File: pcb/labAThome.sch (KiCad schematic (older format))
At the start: 107 parts, among them J1 I2C, J11 24.5.GND.3, J12 NEOPIXEL, J13 Power Input 1, J14 Conn_Coaxial, J15 WS2812_OUT, J2 SRVx, J3 5V, J4 EXT, J5 VPS, J6 FAN2, J7 1wire, J8 1wire, J9 FAN1, K1 G5V-2, K2 G5V-2, K3 G5V-2, M3 SN65HVD230_MODULE, Q1 BC847, Q2 IRLZ44N, Q3 IRLML6344, Q4 BC847, Q5 IRF530, Q6 IRLML5203, SW1 RED, SW2 GREEN, SW4 BLUE, SW5 WHITE, SW7 ROTENC, U1 SR602, U10 MAX3485_MODULE, U11 AM312, U12 24V->4V, U13 LM358, U14 MS4525DO, U15 CCS811_MODULE, U16 24V->5V, U17 DS18B20, U2 TPS5430DDA, U3 Power Input 2, U4 ESP32_DEVKITC_COMPATIBLE, U6 GY-302, U7 Display, U8 MIC, U9 RFM95W-868S2, X1 FAN_6024, m1 Attribution

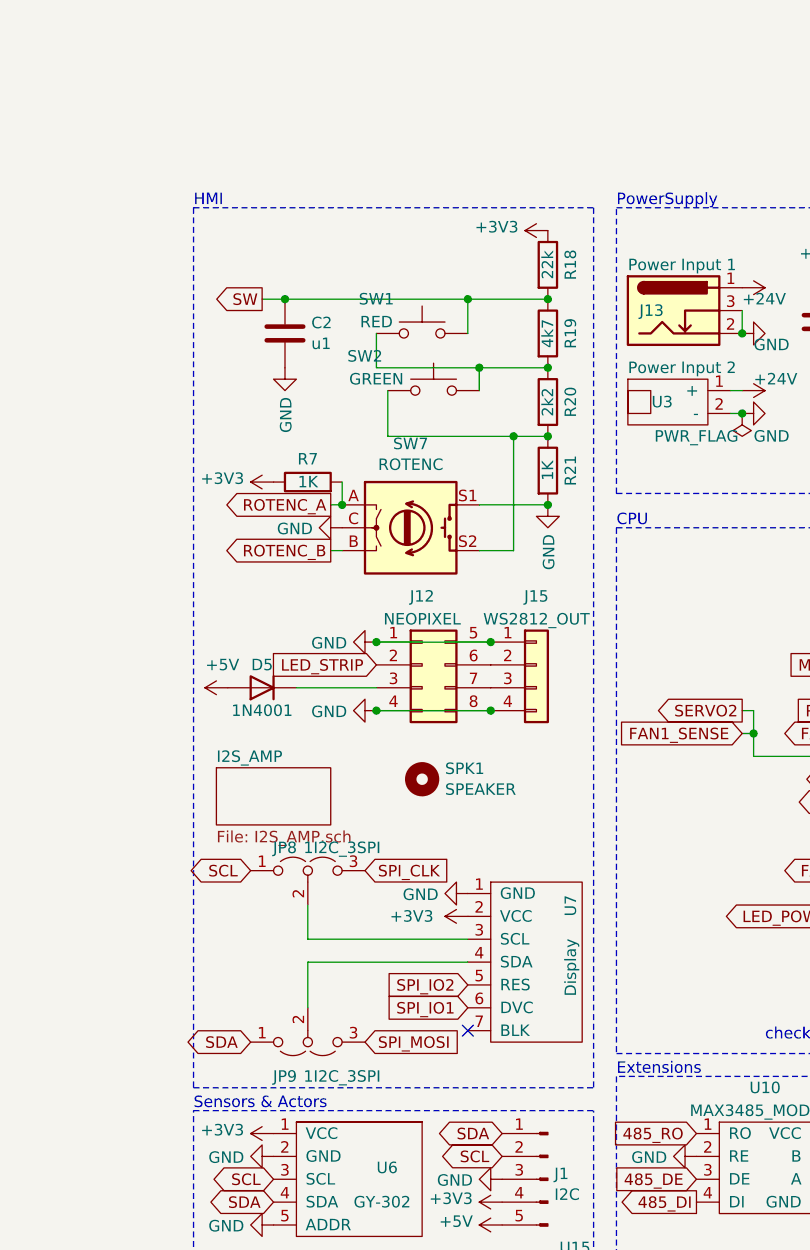
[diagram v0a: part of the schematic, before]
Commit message: I2S-Amp --> Analog (damn cheap) Amp
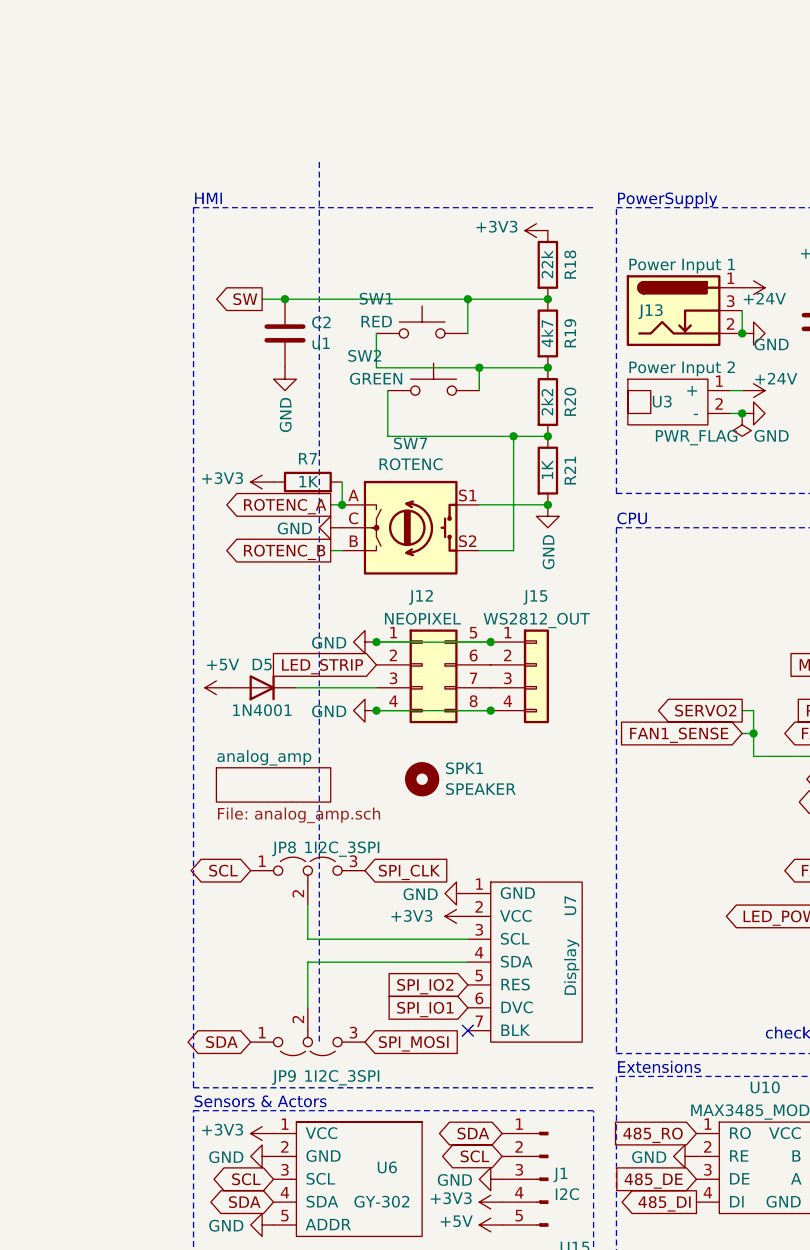
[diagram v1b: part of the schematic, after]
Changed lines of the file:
@@
 $EndComp
 Wire Notes Line
-	2300 600  2300 4450
+	1100 400  1100 4250
 Wire Notes Line
 	550  600  550  4450
@@
 1wire
 $Sheet
-S 650  3050 500  250
-U 60B80D3E
-F0 "I2S_AMP" 50
-F1 "I2S_AMP.sch" 50
+S 650  3050 500  150
+U 60B762EC
+F0 "analog_amp" 50
+F1 "analog_amp.sch" 50
 $EndSheet
 $EndSCHEMATC

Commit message: Minor PCB update
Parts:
- added C15: 100u, liebler_PASSIVES:CP_Elec_6.3x7.7_handsolder, symbol Device:CP
- J12: footprint smopla:NEOPIXEL_STICK_alternativ -> liebler_MODULES:NEOPIXEL_STICK
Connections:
- net GND: now also C15.2
- net at J12.7 (Pin_7), J15.3 (Pin_3): now also C15.1
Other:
- moved on the sheet: D5
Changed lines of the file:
@@
 	1    0    0    -1
 $EndComp
-Wire Notes Line
-	-2800 1850 -2800 5550
 $Comp
 L power:GND #PWR0109
@@
 L power:+5V #PWR051
 U 1 1 5EFC1FD4
-P 700 2700
-F 0 "#PWR051" H 700 2550 50  0001 C CNN
-F 1 "+5V" V 800 2650 50  0000 L CNN
-F 2 "" H 700 2700 50  0001 C CNN
-F 3 "" H 700 2700 50  0001 C CNN
-	1    700  2700
-	0    -1   -1   0
+P 700 2400
+F 0 "#PWR051" H 700 2250 50  0001 C CNN
+F 1 "+5V" V 800 2350 50  0000 L CNN
+F 2 "" H 700 2400 50  0001 C CNN
+F 3 "" H 700 2400 50  0001 C CNN
+	1    700  2400
+	1    0    0    -1
 $EndComp
 $Comp
@@
 P 1350 2800
 F 0 "#PWR052" H 1350 2550 50  0001 C CNN
-F 1 "GND" V 1355 2672 50  0000 R CNN
+F 1 "GND" H 1300 2750 50  0000 R CNN
 F 2 "" H 1350 2800 50  0001 C CNN
 F 3 "" H 1350 2800 50  0001 C CNN
 	1    1350 2800
-	0    1    1    0
+	1    0    0    -1
 $EndComp
 $Comp
@@
 L Diode:1N4001 D5
 U 1 1 5EFF290C
-P 850 2700
-F 0 "D5" H 850 2600 50  0000 C CNN
-F 1 "1N4001" H 850 2800 50  0000 C CNN
-F 2 "Diode_SMD:D_SMA_Handsoldering" H 850 2525 50  0001 C CNN
-F 3 "http://www.vishay.com/docs/88503/1n4001.pdf" H 850 2700 50  0001 C CNN
-	1    850  2700
-	-1   0    0    1
+P 700 2550
+F 0 "D5" H 700 2450 50  0000 C CNN
+F 1 "1N4001" H 700 2650 50  0000 C CNN
+F 2 "Diode_SMD:D_SMA_Handsoldering" H 700 2375 50  0001 C CNN
+F 3 "http://www.vishay.com/docs/88503/1n4001.pdf" H 700 2550 50  0001 C CNN
+	1    700  2550
+	0    -1   -1   0
 $EndComp
 $Comp
@@
 SPI_IO2
 NoConn ~ 1750 4200
-Wire Wire Line
-	1350 2700 1000 2700
 Wire Wire Line
 	7900 3100 7900 3200
@@
 F 0 "J12" H 1550 2900 50  0000 C CNN
 F 1 "NEOPIXEL" H 1550 2800 50  0000 C CNN
-F 2 "smopla:NEOPIXEL_STICK_alternativ" H 1550 2600 50  0001 C CNN
+F 2 "liebler_MODULES:NEOPIXEL_STICK" H 1550 2600 50  0001 C CNN
 F 3 "~" H 1550 2600 50  0001 C CNN
 	1    1550 2600
@@
 $EndComp
 Wire Notes Line
-	1100 400  1100 4250
+	2300 600  2300 4450
 Wire Notes Line
 	550  600  550  4450
@@
 F1 "analog_amp.sch" 50
 $EndSheet
+$Comp
+L Device:CP C15
+U 1 1 60C23DBB
+P 1050 2800
+F 0 "C15" V 1305 2800 50  0000 C CNN
+F 1 "100u" V 1214 2800 50  0000 C CNN
+F 2 "liebler_PASSIVES:CP_Elec_6.3x7.7_handsolder" H 1088 2650 50  0001 C CNN
+F 3 "~" H 1050 2800 50  0001 C CNN
+	1    1050 2800
+	0    -1   -1   0
+$EndComp
+Wire Wire Line
+	1350 2800 1200 2800
+Wire Wire Line
+	700  2700 1350 2700
+Wire Wire Line
+	1850 2700 2150 2700
+Wire Wire Line
+	2150 2700 2150 2950
+Wire Wire Line
+	2150 2950 900  2950
+Wire Wire Line
+	900  2950 900  2800
+Connection ~ 1850 2700
 $EndSCHEMATC

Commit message: labathome V6 as ordered at JLCPCB
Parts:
- added J16: HCP, liebler_CONN:WR_MJ_Modular_Jack_Vertical_Plastic_6P6C, symbol Connector:6P6C
- SW1, SW2, SW4, SW5: footprint Button_Switch_THT:SW_PUSH-12mm -> liebler_MECH:Button_12mm_ANCHOR_CENTER
- SW7: footprint smopla:RotaryEncoder_Alps_EC11E-Switch_Vertical_H20mm -> liebler_MECH:RotaryEncoder_Alps_EC11E-Switch_Vertical_H20mm
- U1: footprint smopla:SR602 -> liebler_MODULES:PIR_Sensor_SR602
- U4: footprint smopla:ESP32_DEVKITC_COMPATIBLE -> liebler_MODULES:ESP32_DEVKITC_COMPATIBLE
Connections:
- net +24V: now also J16.2
- net GND: now also J16.3
- net RS485_A: now reaches U10.6 (A)
- net RS485_A: now also J16.5
- net RS485_B: now reaches U10.7 (B)
- net RS485_B: now also J16.6
- no-connect marks 33 -> 32
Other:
- note added: "A=- B=+"
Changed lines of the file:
@@
 F 0 "SW1" H 1750 1300 50  0000 C CNN
 F 1 "RED" H 1750 1200 50  0000 C CNN
-F 2 "Button_Switch_THT:SW_PUSH-12mm" H 1550 1350 50  0001 C CNN
+F 2 "liebler_MECH:Button_12mm_ANCHOR_CENTER" H 1550 1350 50  0001 C CNN
 F 3 "~" H 1550 1350 50  0001 C CNN
 	1    1550 1150
@@
 F 0 "SW2" H 1300 1550 50  0000 C CNN
 F 1 "GREEN" H 1350 1450 50  0000 C CNN
-F 2 "Button_Switch_THT:SW_PUSH-12mm" H 1600 1600 50  0001 C CNN
+F 2 "liebler_MECH:Button_12mm_ANCHOR_CENTER" H 1600 1600 50  0001 C CNN
 F 3 "~" H 1600 1600 50  0001 C CNN
 	1    1600 1400
@@
 F 0 "SW5" H 10600 6635 50  0000 C CNN
 F 1 "WHITE" H 10600 6544 50  0000 C CNN
-F 2 "Button_Switch_THT:SW_PUSH-12mm" H 10600 6550 50  0001 C CNN
+F 2 "liebler_MECH:Button_12mm_ANCHOR_CENTER" H 10600 6550 50  0001 C CNN
 F 3 "~" H 10600 6550 50  0001 C CNN
 	1    10600 6350
@@
 F 0 "SW4" H 10600 6235 50  0000 C CNN
 F 1 "BLUE" H 10600 6144 50  0000 C CNN
-F 2 "Button_Switch_THT:SW_PUSH-12mm" H 10600 6150 50  0001 C CNN
+F 2 "liebler_MECH:Button_12mm_ANCHOR_CENTER" H 10600 6150 50  0001 C CNN
 F 3 "~" H 10600 6150 50  0001 C CNN
 	1    10600 5950
@@
 F 0 "U4" H 4550 4325 50  0000 C CNN
 F 1 "ESP32_DEVKITC_COMPATIBLE" H 4550 4234 50  0000 C CNN
-F 2 "smopla:ESP32_DEVKITC_COMPATIBLE" H 4550 3050 50  0001 C CNN
+F 2 "liebler_MODULES:ESP32_DEVKITC_COMPATIBLE" H 4550 3050 50  0001 C CNN
 F 3 "" H 4550 3050 50  0001 C CNN
 	1    4550 3200
@@
 F 0 "U1" H 742 7465 50  0000 C CNN
 F 1 "SR602" H 742 7374 50  0000 C CNN
-F 2 "smopla:SR602" H 800 7100 50  0001 C CNN
+F 2 "liebler_MODULES:PIR_Sensor_SR602" H 800 7100 50  0001 C CNN
 F 3 "" H 800 7100 50  0001 C CNN
 	1    800  7100
@@
 	0    1    1    0
 $EndComp
-NoConn ~ 3350 4850
-NoConn ~ 3350 4750
 $Comp
 L power:GND #PWR0116
@@
 F 0 "SW7" H 1500 2367 50  0000 C CNN
 F 1 "ROTENC" H 1500 2276 50  0000 C CNN
-F 2 "smopla:RotaryEncoder_Alps_EC11E-Switch_Vertical_H20mm" H 1350 2160 50  0001 C CNN
+F 2 "liebler_MECH:RotaryEncoder_Alps_EC11E-Switch_Vertical_H20mm" H 1350 2160 50  0001 C CNN
 F 3 "~" H 1500 2260 50  0001 C CNN
 	1    1500 2000
@@
 	900  2950 900  2800
 Connection ~ 1850 2700
+$Comp
+L Connector:6P6C J16
+U 1 1 610E3B2A
+P 12750 3700
+F 0 "J16" H 12807 4267 50  0000 C CNN
+F 1 "HCP" H 12807 4176 50  0000 C CNN
+F 2 "liebler_CONN:WR_MJ_Modular_Jack_Vertical_Plastic_6P6C" V 12750 3725 50  0001 C CNN
+F 3 "~" V 12750 3725 50  0001 C CNN
+	1    12750 3700
+	1    0    0    -1
+$EndComp
+Text Notes 2950 5200 0    50   ~ 0
+A=- B=+
+NoConn ~ 13150 3900
+$Comp
+L power:+24V #PWR0106
+U 1 1 6110EDB7
+P 13150 3800
+F 0 "#PWR0106" H 13150 3650 50  0001 C CNN
+F 1 "+24V" V 13165 3928 50  0000 L CNN
+F 2 "" H 13150 3800 50  0001 C CNN
+F 3 "" H 13150 3800 50  0001 C CNN
+	1    13150 3800
+	0    1    1    0
+$EndComp
+$Comp
+L power:GND #PWR0107
+U 1 1 6110F531
+P 13150 3700
+F 0 "#PWR0107" H 13150 3450 50  0001 C CNN
+F 1 "GND" V 13155 3572 50  0000 R CNN
+F 2 "" H 13150 3700 50  0001 C CNN
+F 3 "" H 13150 3700 50  0001 C CNN
+	1    13150 3700
+	0    -1   -1   0
+$EndComp
+Text GLabel 13150 3500 2    50   Input ~ 0
+RS485_A
+Text GLabel 13150 3400 2    50   Input ~ 0
+RS485_B
+Text Notes 12850 4200 0    50   ~ 0
+A=- B=+
+Text GLabel 3350 4850 2    50   Input ~ 0
+RS485_A
+Text GLabel 3350 4750 2    50   Input ~ 0
+RS485_B
 $EndSCHEMATC

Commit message: Added option description for PCB
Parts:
- C10, C7, C8, C9, D4, L1, R26, R27, U2: Option (none) -> DiscretePSU only
- C3: Option (none) -> LoRaOnly
- C4, C5, D10, D11, D2, D3, D9, Q5, R17, R22, R23, R24, R8, U13: Option (none) -> PowerLED only
- C6: Option (none) -> PressureSensor only
- D1, D12, J9, JP4, Q1, Q2, Q6, R10, R11, R15, R16, R25, R6, R9, X1: Option (none) -> Heater only
- D6, D7, D8, J3, J5, K1, K2, K3, Q4, R1, R12, R13, R14, R2, SW4, SW5: Option (none) -> VPS only
- GSM_Module1, U12, U9: Option (none) -> LoRaWan only
- J16: Option (none) -> HörmannGarage only
- SPK1: Option (none) -> Sound only
- U11: Option (none) -> Alternative PIR only
- U8: Option (none) -> Microphone only

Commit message: pcb V10 as ordered at JLCPCB
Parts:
- R11: footprint smopla:Resistor_100W -> liebler_PASSIVES:Resistor_100W
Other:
- moved on the sheet: J16, U17
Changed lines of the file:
@@
 F 0 "R11" H 6500 900 50  0000 R CNN
 F 1 "22R, 100W" H 6500 1000 50  0000 R CNN
-F 2 "smopla:Resistor_100W" V 6480 950 50  0001 C CNN
+F 2 "liebler_PASSIVES:Resistor_100W" V 6480 950 50  0001 C CNN
 F 3 "~" H 6550 950 50  0001 C CNN
 F 4 "Heater only" H 6550 950 50  0001 C CNN "Option"
@@
 L Sensor_Temperature:DS18B20 U17
 U 1 1 608FDFE2
-P -550 5450
-F 0 "U17" H -780 5496 50  0000 R CNN
-F 1 "DS18B20" H -780 5405 50  0000 R CNN
-F 2 "Package_TO_SOT_THT:TO-92_Inline" H -1550 5200 50  0001 C CNN
-F 3 "http://datasheets.maximintegrated.com/en/ds/DS18B20.pdf" H -700 5700 50  0001 C CNN
-	1    -550 5450
+P 10400 7150
+F 0 "U17" H 10170 7196 50  0000 R CNN
+F 1 "DS18B20" H 10170 7105 50  0000 R CNN
+F 2 "Package_TO_SOT_THT:TO-92_Inline" H 9400 6900 50  0001 C CNN
+F 3 "http://datasheets.maximintegrated.com/en/ds/DS18B20.pdf" H 10250 7400 50  0001 C CNN
+	1    10400 7150
 	1    0    0    -1
 $EndComp
@@
 L power:+3V3 #PWR066
 U 1 1 6090245F
-P -550 5150
-F 0 "#PWR066" H -550 5000 50  0001 C CNN
-F 1 "+3V3" V -535 5278 50  0000 L CNN
-F 2 "" H -550 5150 50  0001 C CNN
-F 3 "" H -550 5150 50  0001 C CNN
-	1    -550 5150
+P 10400 6850
+F 0 "#PWR066" H 10400 6700 50  0001 C CNN
+F 1 "+3V3" V 10415 6978 50  0000 L CNN
+F 2 "" H 10400 6850 50  0001 C CNN
+F 3 "" H 10400 6850 50  0001 C CNN
+	1    10400 6850
 	1    0    0    -1
 $EndComp
@@
 L power:GND #PWR067
 U 1 1 609030A4
-P -550 5750
-F 0 "#PWR067" H -550 5500 50  0001 C CNN
-F 1 "GND" V -545 5622 50  0000 R CNN
-F 2 "" H -550 5750 50  0001 C CNN
-F 3 "" H -550 5750 50  0001 C CNN
-	1    -550 5750
+P 10400 7450
+F 0 "#PWR067" H 10400 7200 50  0001 C CNN
+F 1 "GND" V 10405 7322 50  0000 R CNN
+F 2 "" H 10400 7450 50  0001 C CNN
+F 3 "" H 10400 7450 50  0001 C CNN
+	1    10400 7450
 	1    0    0    -1
 $EndComp
-Text GLabel -250 5450 2    50   BiDi ~ 0
+Text GLabel 10700 7150 2    50   BiDi ~ 0
 1wire
 $Sheet
@@
 L Connector:6P6C J16
 U 1 1 610E3B2A
-P 12750 3700
-F 0 "J16" H 12807 4267 50  0000 C CNN
-F 1 "HCP" H 12807 4176 50  0000 C CNN
-F 2 "liebler_CONN:WR_MJ_Modular_Jack_Vertical_Plastic_6P6C" V 12750 3725 50  0001 C CNN
-F 3 "~" V 12750 3725 50  0001 C CNN
-F 4 "HörmannGarage only" H 12750 3700 50  0001 C CNN "Option"
-	1    12750 3700
+P 8700 7050
+F 0 "J16" H 8757 7617 50  0000 C CNN
+F 1 "HCP" H 8757 7526 50  0000 C CNN
+F 2 "liebler_CONN:WR_MJ_Modular_Jack_Vertical_Plastic_6P6C" V 8700 7075 50  0001 C CNN
+F 3 "~" V 8700 7075 50  0001 C CNN
+F 4 "HörmannGarage only" H 8700 7050 50  0001 C CNN "Option"
+	1    8700 7050
 	1    0    0    -1
 $EndComp
 Text Notes 2950 5200 0    50   ~ 0
 A=- B=+
-NoConn ~ 13150 3900
+NoConn ~ 9100 7250
 $Comp
 L power:+24V #PWR0106
 U 1 1 6110EDB7
-P 13150 3800
-F 0 "#PWR0106" H 13150 3650 50  0001 C CNN
-F 1 "+24V" V 13165 3928 50  0000 L CNN
-F 2 "" H 13150 3800 50  0001 C CNN
-F 3 "" H 13150 3800 50  0001 C CNN
-	1    13150 3800
+P 9100 7150
+F 0 "#PWR0106" H 9100 7000 50  0001 C CNN
+F 1 "+24V" V 9115 7278 50  0000 L CNN
+F 2 "" H 9100 7150 50  0001 C CNN
+F 3 "" H 9100 7150 50  0001 C CNN
+	1    9100 7150
 	0    1    1    0
 $EndComp
@@
 L power:GND #PWR0107
 U 1 1 6110F531
-P 13150 3700
-F 0 "#PWR0107" H 13150 3450 50  0001 C CNN
-F 1 "GND" V 13155 3572 50  0000 R CNN
-F 2 "" H 13150 3700 50  0001 C CNN
-F 3 "" H 13150 3700 50  0001 C CNN
-	1    13150 3700
+P 9100 7050
+F 0 "#PWR0107" H 9100 6800 50  0001 C CNN
+F 1 "GND" V 9105 6922 50  0000 R CNN
+F 2 "" H 9100 7050 50  0001 C CNN
+F 3 "" H 9100 7050 50  0001 C CNN
+	1    9100 7050
 	0    -1   -1   0
 $EndComp
-Text GLabel 13150 3500 2    50   Input ~ 0
+Text GLabel 9100 6850 2    50   Input ~ 0
 RS485_A
-Text GLabel 13150 3400 2    50   Input ~ 0
+Text GLabel 9100 6750 2    50   Input ~ 0
 RS485_B
-Text Notes 12850 4200 0    50   ~ 0
+Text Notes 8800 7550 0    50   ~ 0
 A=- B=+
 Text GLabel 3350 4850 2    50   Input ~ 0
